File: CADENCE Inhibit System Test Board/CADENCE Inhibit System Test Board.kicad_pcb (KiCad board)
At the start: 2 copper layers, 70 x 95 mm, 55 parts, among them IC1 LTC7004IMSE#WTRPBF, IC2 LTC7004IMSE#WTRPBF, IC3 LTC7004IMSE#WTRPBF, IC4 LTC7004IMSE#WTRPBF, IC5 LTC7004IMSE#WTRPBF, J1 INHIBIT_P2, J10 Conn_01x04, J11 Conn_01x02, J2 INHIBIT_P2, J3 INHIBIT_P2, J4 INHIBIT_P2, J5 INHIBIT_P2, J6 INHIBIT_P2, J7 INHIBIT_P2, J8 INHIBIT_P2, J9 INHIBIT_P2, Q1 SUD23N06-31-GE3, Q2 SUD23N06-31-GE3, Q3 SUD23N06-31-GE3, Q4 SUD23N06-31-GE3, Q5 SUD23N06-31-GE3, Q6 SUD23N06-31-GE3, Q7 SUD23N06-31-GE3, U1 MIC4427YM-TR, U2 MIC4427YM-TR

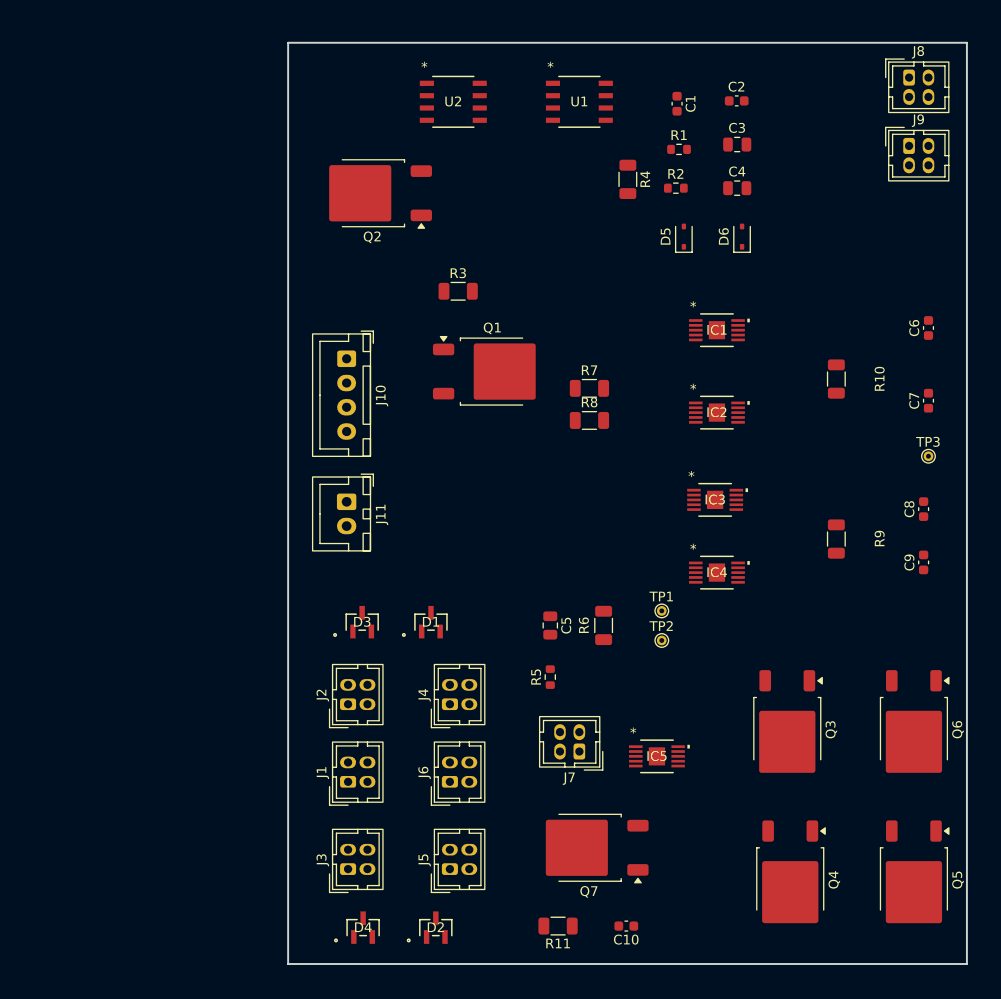
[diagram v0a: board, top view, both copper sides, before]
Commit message: pcb layout
confident in completion of IC3, IC4, IC1, foot switches, and low power side
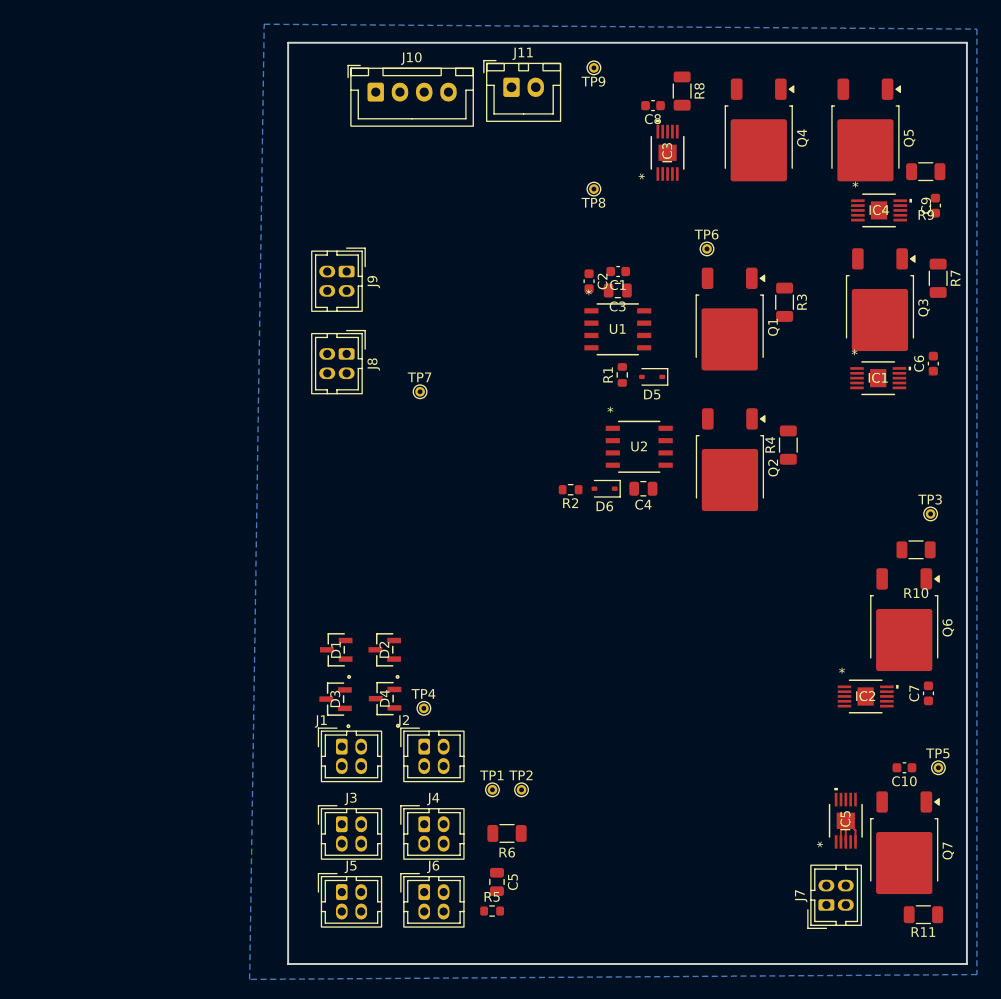
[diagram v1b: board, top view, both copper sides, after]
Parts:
- added TP4: Voltage Level, TestPoint:TestPoint_THTPad_D1.0mm_Drill0.5mm, F.Cu at (134.5, 112.5)
- added TP5: UNREG, TestPoint:TestPoint_THTPad_D1.0mm_Drill0.5mm, F.Cu at (187.5, 118.7)
- added TP6: Cell 3-, TestPoint:TestPoint_THTPad_D1.0mm_Drill0.5mm, F.Cu at (163.7, 65.2)
- added TP7: VSS, TestPoint:TestPoint_THTPad_D1.0mm_Drill0.5mm, F.Cu at (134.1, 79.9)
- added TP8: V_mppt_o, TestPoint:TestPoint_THTPad_D1.0mm_Drill0.5mm, F.Cu at (152.0, 59.0)
- added TP9: V_mppt_i, TestPoint:TestPoint_THTPad_D1.0mm_Drill0.5mm, F.Cu at (152.0, 46.5)
- moved Q5 76.7 mm to (180.0, 53.7)
- moved Q4 76.6 mm to (169.0, 53.7)
- moved J8 64.6 mm to (126.5, 76.0), turned to -90 degrees
- moved J9 59.4 mm to (126.5, 67.5), turned to -90 degrees
- moved C8 50.1 mm to (158.1, 50.4), turned to 180 degrees
- moved Q2 46.5 mm to (166.0, 87.7), turned to -90 degrees
- moved J11 46.0 mm to (143.5, 48.5), turned to 0 degrees
- moved Q3 44.5 mm to (181.5, 71.2)
- moved IC4 40.9 mm to (181.4, 61.2)
- moved U2 40.4 mm to (156.7, 85.6)
- moved R9 39.0 mm to (186.2, 57.2), turned to 180 degrees
- moved R7 37.7 mm to (187.5, 68.2), turned to -90 degrees
- moved R11 37.7 mm to (186.0, 133.8)
- moved C9 36.8 mm to (187.2, 60.7)
- moved IC3 36.1 mm to (159.6, 55.3), turned to 90 degrees
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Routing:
- net VSS: track 0.00 -> 7.17 mm
- added copper zone on B.Cu, net VSS

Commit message: PCB Updates: added traces
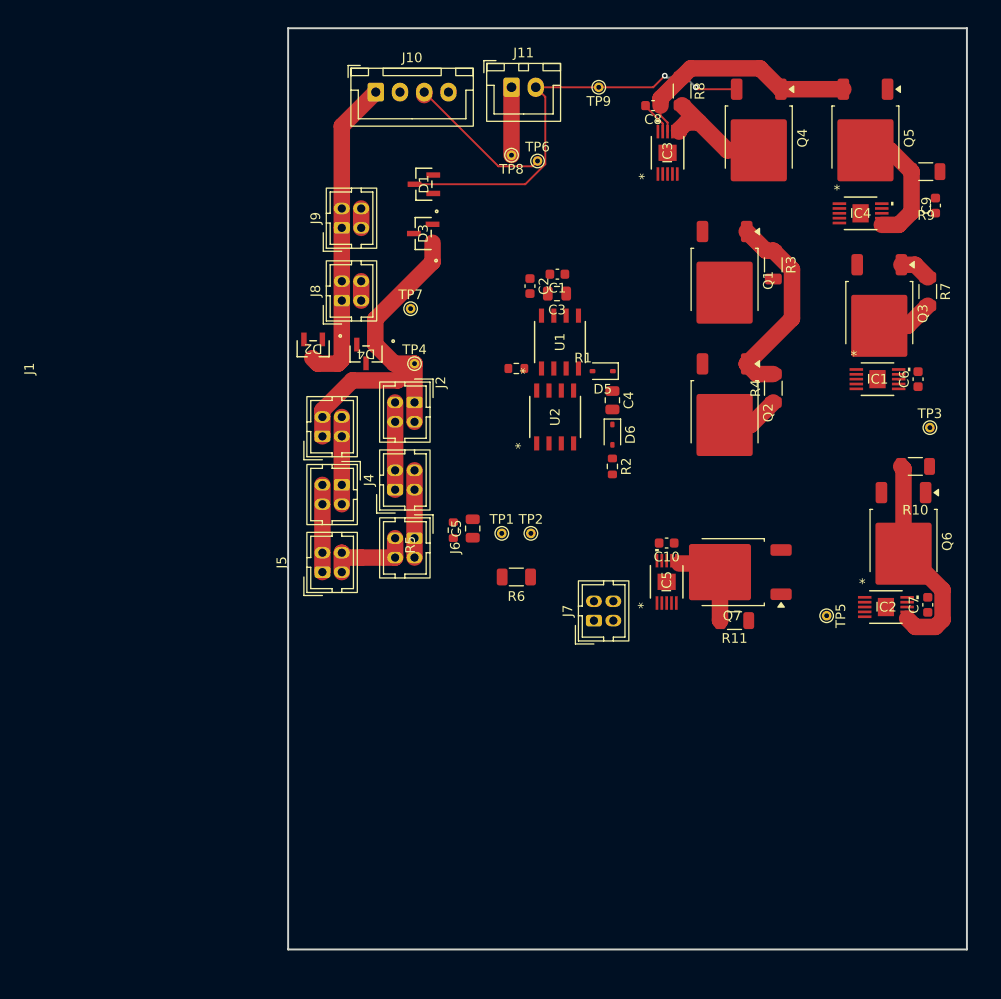
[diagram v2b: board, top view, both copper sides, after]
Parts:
- moved D3 48.9 mm to (134.4, 63.6)
- moved D1 48.9 mm to (134.5, 58.5)
- moved R5 39.5 mm to (137.5, 94.2), turned to 90 degrees
- moved J7 37.9 mm to (152.0, 103.5)
- moved C5 36.5 mm to (139.5, 94.0), turned to 90 degrees
- moved J6 36.5 mm to (133.5, 95.0), turned to -90 degrees
- moved R11 36.0 mm to (166.5, 103.5)
- moved D4 35.6 mm to (128.5, 76.0), turned to 180 degrees
- moved TP4 35.6 mm to (133.5, 77.0)
- moved J2 35.5 mm to (133.5, 81.0), turned to -90 degrees
- moved J3 35.0 mm to (126.0, 89.5), turned to -90 degrees
- moved J4 34.6 mm to (131.5, 90.0), turned to 90 degrees
- moved Q7 33.8 mm to (166.3, 98.5), turned to 180 degrees
- moved C10 33.7 mm to (159.5, 95.5)
- moved J5 33.1 mm to (124.0, 98.5), turned to 90 degrees
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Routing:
- net V_mppt_i: track 0.00 -> 44.5 mm, vias 0 -> 2
- net Net-(D3-K): track 0.00 -> 38.0 mm
- net Cell 1+: track 0.00 -> 32.5 mm
- net Net-(IC3-TS): track 0.00 -> 24.7 mm
- net Net-(IC2-TGDN): track 0.00 -> 22.1 mm
- net Net-(Q1-S): track 0.00 -> 21.1 mm
- net Cell 3-: track 0.00 -> 15.4 mm
- net Net-(IC4-TGDN): track 0.00 -> 13.5 mm
- net Net-(IC3-TGDN): track 0.00 -> 12.4 mm
- net Net-(J5-Pin_2): track 0.00 -> 9.71 mm
- net Net-(IC5-TGDN): track 0.00 -> 9.59 mm
- net Net-(J2-Pin_2): track 0.00 -> 9.50 mm
- net Net-(J4-Pin_2): track 0.00 -> 9.00 mm
- net Net-(J3-Pin_2): track 0.00 -> 9.00 mm
- net Net-(J1-Pin_2): track 0.00 -> 9.00 mm
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- removed copper zone on B.Cu, net VSS

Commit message: tracing more
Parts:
- moved C7 3.98 mm to (183.9, 98.8), turned to 180 degrees
- moved TP5 3.08 mm to (172.9, 102.9)
- moved Q6 2.75 mm to (183.9, 92.6)
- moved R10 2.75 mm to (185.2, 84.9)
- moved IC2 2.57 mm to (184.4, 103.3), turned to 90 degrees
- moved R1 2.02 mm to (143.8, 75.5)
- moved TP3 1.77 mm to (186.6, 81.8)
- moved C10 1.26 mm to (158.2, 95.5)
- moved IC5 1.26 mm to (158.2, 99.5)
- moved J7 1.26 mm to (150.7, 103.5)
- moved Q7 1.26 mm to (165.0, 98.5)
- moved R11 1.26 mm to (165.2, 103.5)
- moved D2 1.12 mm to (123.8, 76.3), turned to 90 degrees
- moved IC1 1.01 mm to (181.4, 77.6)
- moved C6 1.01 mm to (185.5, 77.6)
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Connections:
- Q3 pad 1: Net-(IC1-TS) -> Cell 1+
- Q3 pad 3: Cell 1+ -> Net-(IC1-TS)
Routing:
- net HIGH_SIDE_PWR: track 2.00 -> 106.1 mm, vias 0 -> 10
- net Cell 1+: track 32.5 -> 124.7 mm, vias 0 -> 4
- net UNREG: track 0.00 -> 83.6 mm, vias 0 -> 2
- net V_mppt_o: track 7.00 -> 75.4 mm, vias 0 -> 2
- net EN: track 0.48 -> 61.0 mm
- net LOW_SIDE_PWR: track 2.00 -> 62.0 mm, vias 0 -> 4
- net Net-(IC2-TS): track 0.00 -> 37.8 mm, vias 0 -> 2
- net Net-(IC1-TS): track 3.32 -> 34.9 mm
- net Net-(Q1-G): track 0.00 -> 26.2 mm
- net Net-(Q2-G): track 5.99 -> 27.1 mm
- net Cell 3-: track 15.4 -> 34.6 mm, vias 0 -> 1
- net Net-(D6-A): track 0.00 -> 11.8 mm
- net Net-(D5-A): track 0.00 -> 11.5 mm
- net Net-(IC1-TGDN): track 5.86 -> 16.3 mm
- net Net-(IC5-INP): track 0.00 -> 9.30 mm
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- added copper zone on B.Cu, net VSS
- added copper zone on F.Cu, net VSS

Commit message: Continued adding traces for gnd
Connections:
- IC5 pad 1: Cell 1+ -> HIGH_SIDE_PWR
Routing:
- net VSS: track 0.12 -> 66.8 mm, vias 0 -> 24
- net HIGH_SIDE_PWR: track 106.1 -> 134.6 mm, vias 10 -> 15
- net Cell 1+: track 124.7 -> 118.4 mm
- net (no net): track 2.88 -> 0.00 mm
- net V_mppt_o: vias 2 -> 4

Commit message: finished connections and added vias
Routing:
- net EN: track 61.0 -> 164.7 mm, vias 0 -> 9
- net VSS: track 66.8 -> 82.0 mm, vias 24 -> 67
- net Net-(IC2-TGDN): track 17.9 -> 23.1 mm
- net Cell 3-: track 34.6 -> 34.8 mm, vias 1 -> 0
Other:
- board text added: "BMS General"
- board text added: "Foot Switches"
- board text added: "Solar Charger"

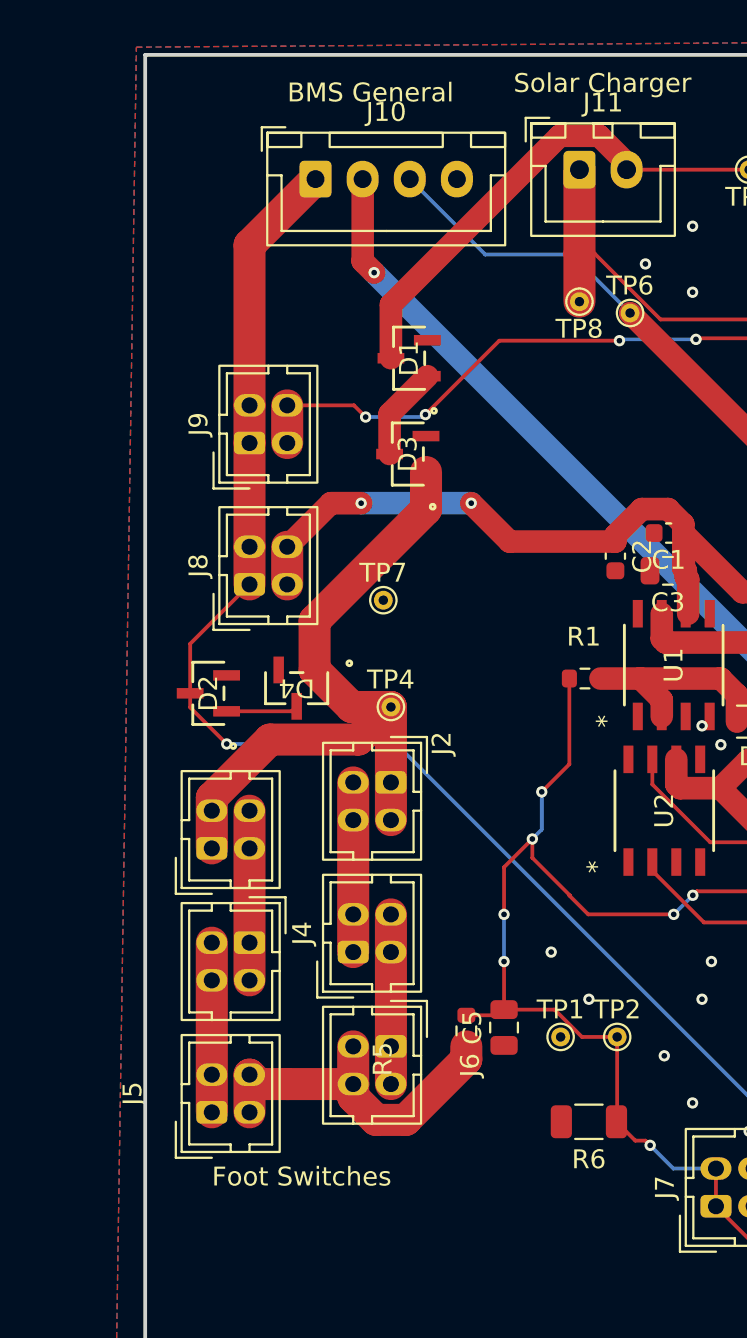
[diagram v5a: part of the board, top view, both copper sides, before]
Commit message: pcb silkscreens
i did a bit :p
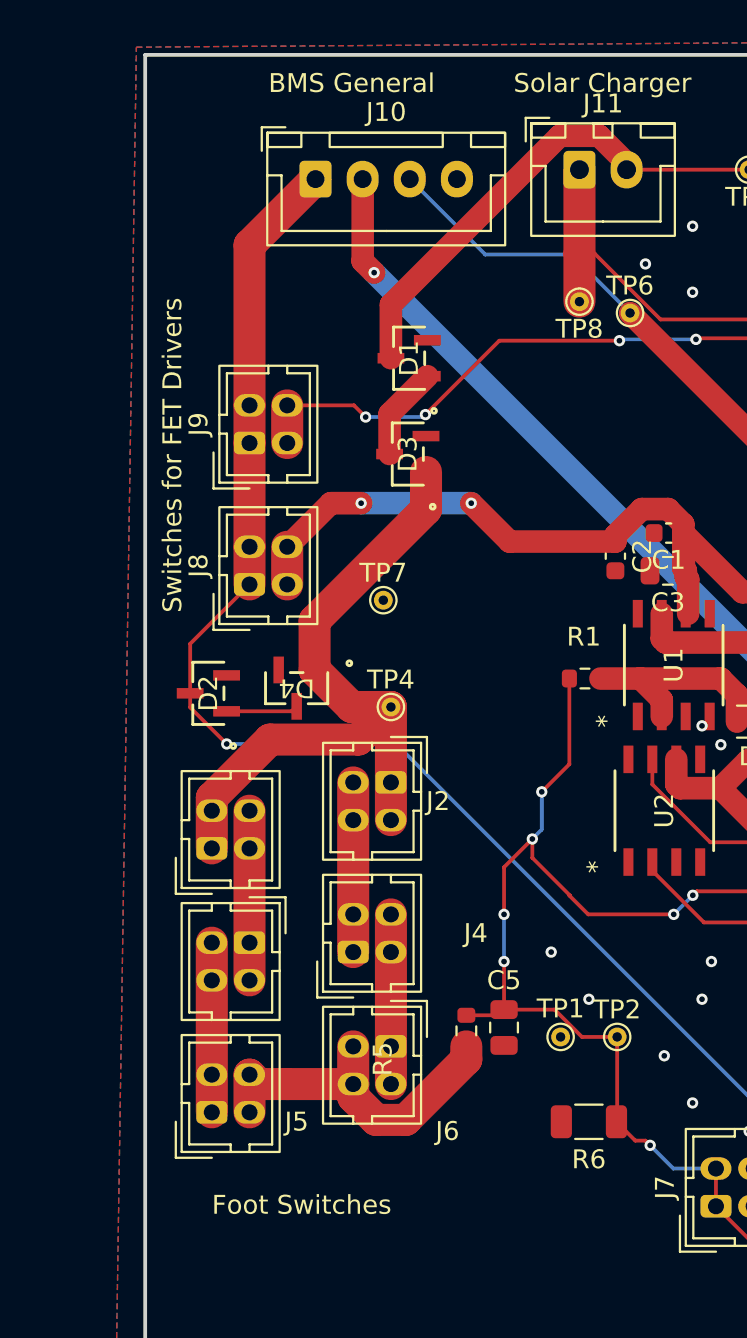
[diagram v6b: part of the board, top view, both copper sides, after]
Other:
- board text added: "Switches for FET Drivers"
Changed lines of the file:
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@@
 		(tags "connector JST XH vertical")
 		(property "Reference" "J11"
-			(at 1.25 -3.55 0)
+			(at 1.25 -3.5 0)
 			(layer "F.SilkS")
 			(effects
@@
 		(tags "test point THT pad")
 		(property "Reference" "TP1"
-			(at 0 -1.448 0)
+			(at 0 -1.5 0)
 			(layer "F.SilkS")
 			(effects
@@
 		)
 		(property "Value" "VSS"
-			(at 0 1.55 0)
+			(at 0 2 180)
 			(layer "F.Fab")
 			(effects
@@
 		(tags "connector Hirose DF11 vertical")
 		(property "Reference" "J5"
-			(at 1 -4.2 90)
+			(at -0.5 4.5 180)
 			(layer "F.SilkS")
 			(effects
@@
 		)
 		(property "Value" "INHIBIT_P2"
-			(at 1 4.7 90)
+			(at -3.5 1 180)
 			(layer "F.Fab")
 			(effects
@@
 		)
 		(property "Value" "EN"
-			(at 0 1.55 0)
+			(at 0 2 0)
 			(layer "F.Fab")
 			(effects
@@
 		(tags "connector Hirose DF11 vertical")
 		(property "Reference" "J2"
-			(at -2.0696 -2.7 90)
+			(at 1 -2.5 180)
 			(layer "F.SilkS")
 			(effects
@@
 		)
 		(property "Value" "INHIBIT_P2"
-			(at 1 4.7 90)
+			(at 1.5 4.7 90)
 			(layer "F.Fab")
 			(effects
@@
 		)
 		(property "Value" "100k"
-			(at 0 1.83 0)
+			(at 0 -3.5 0)
 			(layer "F.Fab")
 			(effects
@@
 		)
 		(property "Value" "39k"
-			(at 0 1.43 90)
+			(at -2.825 0 90)
 			(layer "F.Fab")
 			(effects
@@
 		)
 		(property "Value" "Voltage Level"
-			(at 0 1.55 0)
+			(at 4.5 5.5 90)
 			(layer "F.Fab")
 			(effects
@@
 		)
 		(property "Value" "MMBD914LT1G"
-			(at -8.0475 0 90)
+			(at -1.2248 -2.8175 90)
 			(unlocked yes)
 			(layer "F.Fab")
@@
 		(tags "connector Hirose DF11 vertical")
 		(property "Reference" "J6"
-			(at 1 -4.2 90)
+			(at 4.5 -3 180)
 			(layer "F.SilkS")
 			(effects
@@
 		)
 		(property "Value" "INHIBIT_P2"
-			(at 1 4.7 90)
+			(at 6 0 180)
 			(layer "F.Fab")
 			(effects
@@
 		)
 		(property "Value" "INHIBIT_P2"
-			(at 1 4.7 90)
+			(at 2.5 4.7 90)
 			(layer "F.Fab")
 			(effects
@@
 		)
 		(property "Value" "INHIBIT_P2"
-			(at 1 4.7 90)
+			(at 0.5 -3 90)
 			(layer "F.Fab")
 			(effects
@@
 		(tags "connector Hirose DF11 vertical")
 		(property "Reference" "J4"
-			(at 1 -2.7 90)
+			(at 1 6.5 180)
 			(layer "F.SilkS")
 			(effects
@@
 		(tags "capacitor")
 		(property "Reference" "C5"
-			(at 0 -1.68 90)
+			(at 2.5 0 180)
 			(layer "F.SilkS")
 			(effects
@@
 		)
 		(property "Value" "10nF"
-			(at -3 1.68 90)
+			(at -3.5 0 90)
 			(layer "F.Fab")
 			(effects
@@
 	)
 	(gr_text "Foot Switches"
-		(at 124 102.5 0)
+		(at 124 104 0)
 		(layer "F.SilkS")
 		(effects
@@
 	)
 	(gr_text "BMS General"
-		(at 128 45 0)
+		(at 127 44.5 0)
 		(layer "F.SilkS")
 		(effects
@@
 		(layer "F.SilkS")
 		(effects
+			(font
+				(size 1 1)
+				(thickness 0.1)
+			)
+			(justify left bottom)
+		)
+	)
+	(gr_text "Switches for FET Drivers"
+		(at 122.5 72 90)
+		(layer "F.SilkS")
+		(effects
